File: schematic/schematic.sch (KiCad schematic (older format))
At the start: 22 parts, among them J1 Conn_01x04, J19 Conn_02x05_Odd_Even, J2 Conn_01x04, J20 Conn_02x05_Odd_Even, J21 Conn_02x05_Odd_Even, J3 Conn_01x04, J4 Conn_01x04, J5 Conn_01x04, SW1 SW_Push_Dual, U1 STM32F401VETx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

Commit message: Updated to kicad 5.0.0
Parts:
- C1, C2, C3, C4, C5: symbol C -> Device:C
- J1, J2, J3, J4, J5: symbol Conn_01x04 -> Connector_Generic:Conn_01x04
- J19, J20, J21: symbol Conn_02x05_Odd_Even -> Connector_Generic:Conn_02x05_Odd_Even
- MK1, MK2, MK3, MK4: symbol Mounting_Hole -> Mechanical:Mounting_Hole
- R1, R2: symbol R -> Device:R
- SW1: symbol SW_Push_Dual -> Switch:SW_Push_Dual
- U1: symbol STM32F401VETx -> MCU_ST_STM32:STM32F401VETx
- Y1: symbol Crystal_GND24 -> Device:Crystal_GND24
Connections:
- no-connect marks 4 -> 15

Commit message: Revert "Updated to kicad 5.0.0"
This reverts commit 6c14fa6c8e6361c9b9ee4065803a5a63755fc6a7.
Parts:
- C1, C2, C3, C4, C5: symbol Device:C -> C
- J1, J2, J3, J4, J5: symbol Connector_Generic:Conn_01x04 -> Conn_01x04
- J19, J20, J21: symbol Connector_Generic:Conn_02x05_Odd_Even -> Conn_02x05_Odd_Even
- MK1, MK2, MK3, MK4: symbol Mechanical:Mounting_Hole -> Mounting_Hole
- R1, R2: symbol Device:R -> R
- SW1: symbol Switch:SW_Push_Dual -> SW_Push_Dual
- U1: symbol MCU_ST_STM32:STM32F401VETx -> STM32F401VETx
- Y1: symbol Device:Crystal_GND24 -> Crystal_GND24
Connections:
- no-connect marks 15 -> 4

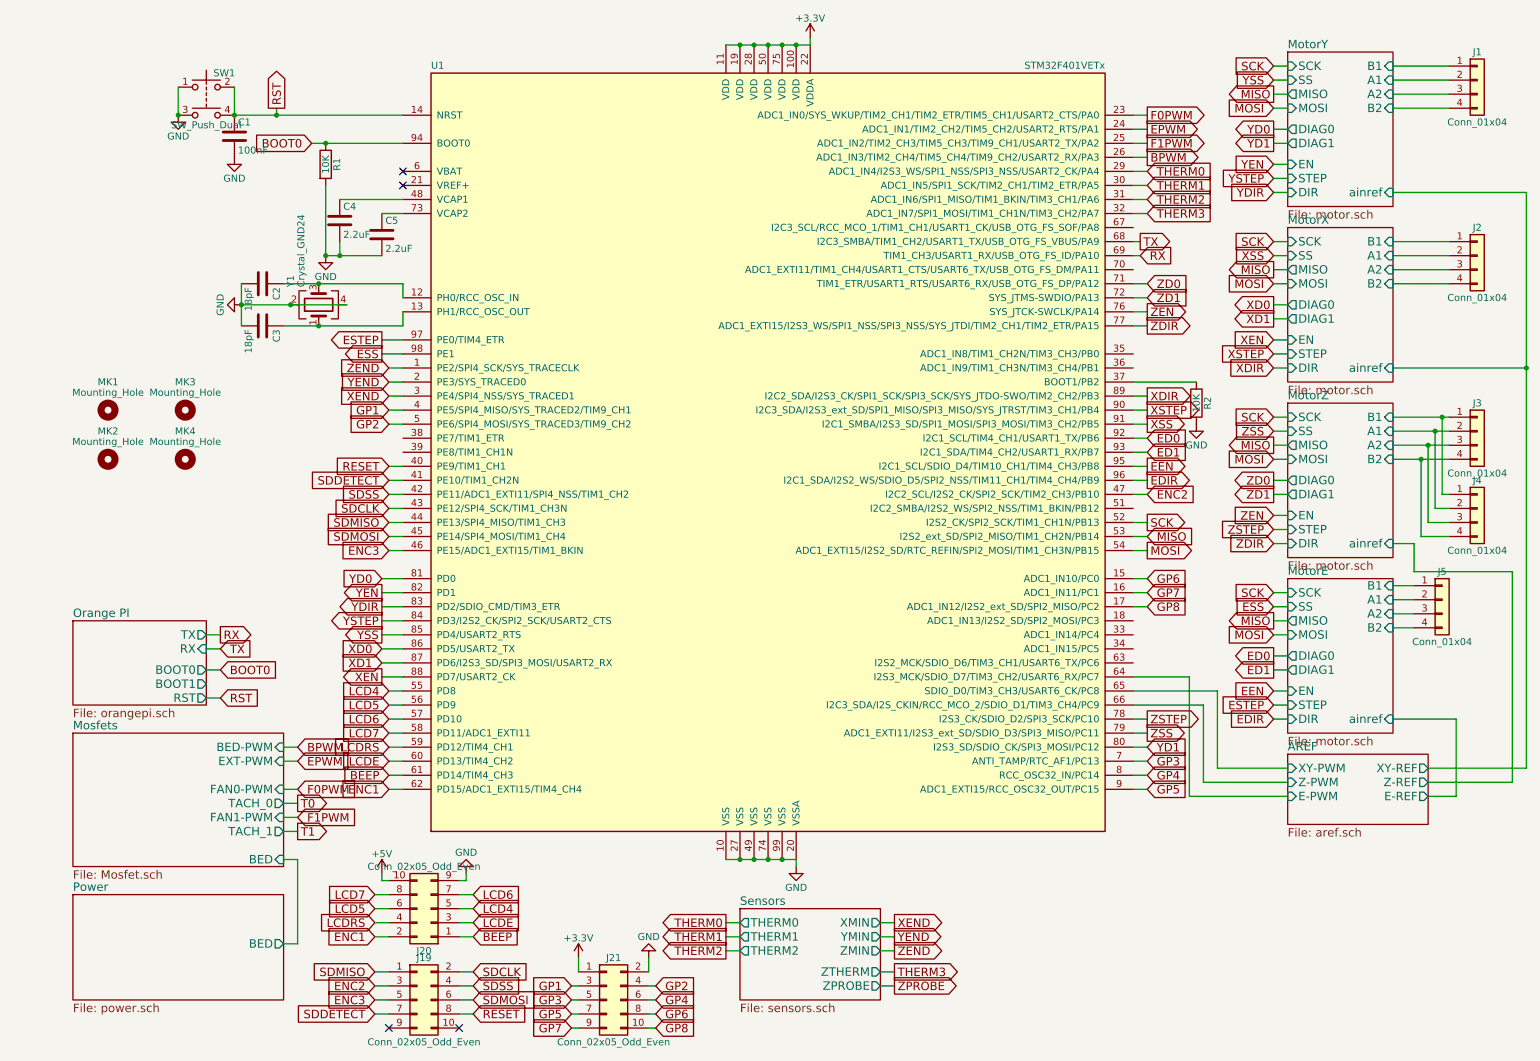
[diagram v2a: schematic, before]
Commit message: Removed some components
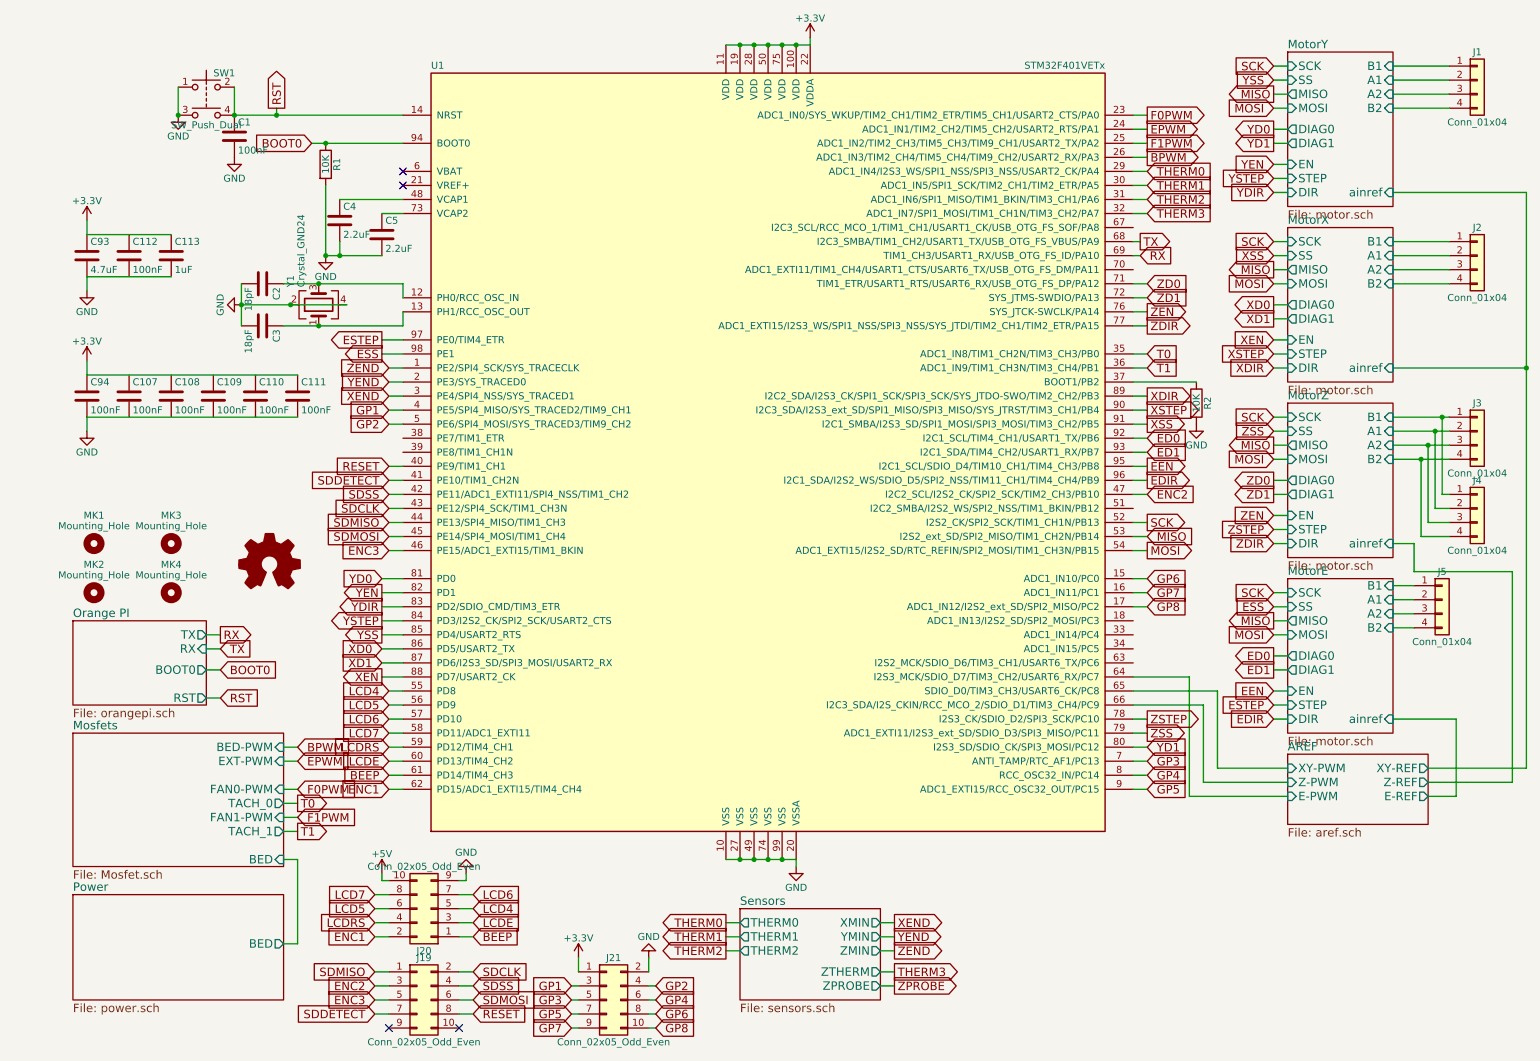
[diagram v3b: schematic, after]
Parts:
- added C107, C108, C109, C110, C111, C112: 100nF, Capacitors_SMD:C_0603, symbol C
- added C113: 1uF, Capacitors_SMD:C_0603, symbol C
- added C93: 4.7uF, Capacitors_SMD:C_0603, symbol C
- added C94: 100nF, Capacitor_SMD:C_0603_1608Metric, symbol C
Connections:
- net +3V3: now also C111.1, C113.1, C93.1, C94.1
- net GND: now also C111.2, C113.2, C93.2, C94.2
- net T0: now also U1.35 (ADC1_IN8/TIM1_CH2N/TIM3_CH3/PB0)
- net T1: now also U1.36 (ADC1_IN9/TIM1_CH3N/TIM3_CH4/PB1)
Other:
- moved on the sheet: MK1, MK2, MK3, MK4

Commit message: Added logo's and stm32 capacitors
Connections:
- net +3V3: now also C107.1, C108.1, C109.1, C110.1, C112.1, U1.21 (VREF+)
- net GND: now also C107.2, C108.2, C109.2, C110.2, C112.2
- no-connect marks 4 -> 3
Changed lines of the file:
@@
 EESchema Schematic File Version 2
+LIBS:bd9e302efj
+LIBS:psmn1
+LIBS:tmc2130
 LIBS:74xgxx
 LIBS:74xx
@@
 LIBS:zetex
 LIBS:Zilog
-LIBS:bd9e302efj
-LIBS:psmn1
-LIBS:tmc2130
 LIBS:schematic-cache
 EELAYER 25 0
@@
 $EndComp
 $Comp
-L GND #PWR11
+L GND #PWR01
 U 1 1 59F126EE
 P 5700 6500
-F 0 "#PWR11" H 5700 6250 50  0001 C CNN
+F 0 "#PWR01" H 5700 6250 50  0001 C CNN
 F 1 "GND" H 5700 6350 50  0000 C CNN
 F 2 "" H 5700 6500 50  0001 C CNN
@@
 $EndComp
 $Comp
-L +3.3V #PWR1
+L +3.3V #PWR02
 U 1 1 59F1505F
 P 5800 600
-F 0 "#PWR1" H 5800 450 50  0001 C CNN
+F 0 "#PWR02" H 5800 450 50  0001 C CNN
 F 1 "+3.3V" H 5800 740 50  0000 C CNN
 F 2 "" H 5800 600 50  0001 C CNN
@@
 $EndComp
 $Comp
-L GND #PWR7
+L GND #PWR03
 U 1 1 59EF5034
 P 1750 2500
-F 0 "#PWR7" H 1750 2250 50  0001 C CNN
+F 0 "#PWR03" H 1750 2250 50  0001 C CNN
 F 1 "GND" H 1750 2350 50  0000 C CNN
 F 2 "" H 1750 2500 50  0001 C CNN
@@
 $EndComp
 $Comp
-L GND #PWR5
+L GND #PWR04
 U 1 1 59F2A2E0
 P 2350 2150
-F 0 "#PWR5" H 2350 1900 50  0001 C CNN
+F 0 "#PWR04" H 2350 1900 50  0001 C CNN
 F 1 "GND" H 2350 2000 50  0000 C CNN
 F 2 "" H 2350 2150 50  0001 C CNN
@@
 $EndComp
 $Comp
-L GND #PWR9
+L GND #PWR05
 U 1 1 59F2ED55
 P 8550 3350
-F 0 "#PWR9" H 8550 3100 50  0001 C CNN
+F 0 "#PWR05" H 8550 3100 50  0001 C CNN
 F 1 "GND" H 8550 3200 50  0000 C CNN
 F 2 "" H 8550 3350 50  0001 C CNN
@@
 $EndComp
 $Comp
-L GND #PWR2
+L GND #PWR06
 U 1 1 59F30F85
 P 1300 1150
-F 0 "#PWR2" H 1300 900 50  0001 C CNN
+F 0 "#PWR06" H 1300 900 50  0001 C CNN
 F 1 "GND" H 1300 1000 50  0000 C CNN
 F 2 "" H 1300 1150 50  0001 C CNN
@@
 $EndComp
 $Comp
-L GND #PWR3
+L GND #PWR07
 U 1 1 59F319C0
 P 1700 1450
-F 0 "#PWR3" H 1700 1200 50  0001 C CNN
+F 0 "#PWR07" H 1700 1200 50  0001 C CNN
 F 1 "GND" H 1700 1300 50  0000 C CNN
 F 2 "" H 1700 1450 50  0001 C CNN
@@
 RST
 NoConn ~ 2900 1550
-NoConn ~ 2900 1650
 Text GLabel 8150 2050 2    60   Output ~ 0
 TX
@@
 $EndComp
 $Comp
-L +5V #PWR12
+L +5V #PWR08
 U 1 1 5A71CAE9
 P 2750 6550
-F 0 "#PWR12" H 2750 6400 50  0001 C CNN
+F 0 "#PWR08" H 2750 6400 50  0001 C CNN
 F 1 "+5V" H 2750 6690 50  0000 C CNN
 F 2 "" H 2750 6550 50  0001 C CNN
@@
 $EndComp
 $Comp
-L GND #PWR13
+L GND #PWR09
 U 1 1 5A71CE27
 P 3350 6550
-F 0 "#PWR13" H 3350 6300 50  0001 C CNN
+F 0 "#PWR09" H 3350 6300 50  0001 C CNN
 F 1 "GND" H 3350 6400 50  0000 C CNN
 F 2 "" H 3350 6550 50  0001 C CNN
@@
 $EndComp
 $Comp
-L +3.3V #PWR14
+L +3.3V #PWR010
 U 1 1 5A764DEA
 P 4150 7150
-F 0 "#PWR14" H 4150 7000 50  0001 C CNN
+F 0 "#PWR010" H 4150 7000 50  0001 C CNN
 F 1 "+3.3V" H 4150 7290 50  0000 C CNN
 F 2 "" H 4150 7150 50  0001 C CNN
@@
 $EndComp
 $Comp
-L GND #PWR15
+L GND #PWR011
 U 1 1 5A76523A
 P 4650 7150
-F 0 "#PWR15" H 4650 6900 50  0001 C CNN
+F 0 "#PWR011" H 4650 6900 50  0001 C CNN
 F 1 "GND" H 4650 7000 50  0000 C CNN
 F 2 "" H 4650 7150 50  0001 C CNN
@@
 	8100 2950 8200 2950
 $Comp
-L GND #PWR10
+L GND #PWR012
 U 1 1 5ADF511D
 P 650 3400
-F 0 "#PWR10" H 650 3150 50  0001 C CNN
+F 0 "#PWR012" H 650 3150 50  0001 C CNN
 F 1 "GND" H 650 3250 50  0000 C CNN
 F 2 "" H 650 3400 50  0001 C CNN
@@
 $EndComp
 $Comp
-L +3.3V #PWR8
+L +3.3V #PWR013
 U 1 1 5ADF71B2
 P 650 2900
-F 0 "#PWR8" H 650 2750 50  0001 C CNN
+F 0 "#PWR013" H 650 2750 50  0001 C CNN
 F 1 "+3.3V" H 650 3040 50  0000 C CNN
 F 2 "" H 650 2900 50  0001 C CNN
@@
 F 0 "#LOGO1" H 1950 4625 50  0001 C CNN
 F 1 "Logo_Open_Hardware_Small" H 1950 4125 50  0001 C CNN
-F 2 "" H 1950 4350 50  0001 C CNN
+F 2 "Symbols:OSHW-Logo_11.4x12mm_SilkScreen" H 1950 4350 50  0001 C CNN
 F 3 "" H 1950 4350 50  0001 C CNN
 	1    1950 4350
@@
 	650  3000 2150 3000
 $Comp
-L GND #PWR6
+L GND #PWR014
 U 1 1 5AE06323
 P 650 2400
-F 0 "#PWR6" H 650 2150 50  0001 C CNN
+F 0 "#PWR014" H 650 2150 50  0001 C CNN
 F 1 "GND" H 650 2250 50  0000 C CNN
 F 2 "" H 650 2400 50  0001 C CNN
@@
 $EndComp
 $Comp
-L +3.3V #PWR4
+L +3.3V #PWR015
 U 1 1 5AE06329
 P 650 1900
-F 0 "#PWR4" H 650 1750 50  0001 C CNN
+F 0 "#PWR015" H 650 1750 50  0001 C CNN
 F 1 "+3.3V" H 650 2040 50  0000 C CNN
 F 2 "" H 650 1900 50  0001 C CNN
@@
 Wire Wire Line
 	650  2300 1250 2300
+Connection ~ 650  3000
+Connection ~ 950  3000
+Connection ~ 1250 3000
+Connection ~ 1550 3000
+Connection ~ 1850 3000
+Connection ~ 950  3300
+Connection ~ 1250 3300
+Connection ~ 1550 3300
+Connection ~ 1850 3300
+Connection ~ 950  2000
+Connection ~ 950  2300
+Connection ~ 650  2000
+Connection ~ 650  2300
+Connection ~ 650  3300
+Wire Wire Line
+	2900 1650 2650 1650
+$Comp
+L +3.3V #PWR016
+U 1 1 5ADE5ADE
+P 2650 1650
+F 0 "#PWR016" H 2650 1500 50  0001 C CNN
+F 1 "+3.3V" H 2650 1790 50  0000 C CNN
+F 2 "" H 2650 1650 50  0001 C CNN
+F 3 "" H 2650 1650 50  0001 C CNN
+	1    2650 1650
+	1    0    0    -1
+$EndComp
 $EndSCHEMATC

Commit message: Saved schematic
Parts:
- C94: footprint Capacitor_SMD:C_0603_1608Metric -> Capacitors_SMD:C_0603
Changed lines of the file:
@@
 F 0 "C94" H 675 3250 50  0000 L CNN
 F 1 "100nF" H 675 3050 50  0000 L CNN
-F 2 "Capacitor_SMD:C_0603_1608Metric" H 688 3000 50  0001 C CNN
+F 2 "Capacitors_SMD:C_0603" H 688 3000 50  0001 C CNN
 F 3 "" H 650 3150 50  0001 C CNN
 	1    650  3150

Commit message: Updated to kicad v5
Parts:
- C1, C107, C108, C109, C110, C111, C112, C113, C2, C3, C4, C5, C93, C94: symbol C -> schematic-rescue:C
- J1, J2, J3, J4, J5: symbol Conn_01x04 -> schematic-rescue:Conn_01x04
- J19, J20, J21: symbol Conn_02x05_Odd_Even -> schematic-rescue:Conn_02x05_Odd_Even
- MK1, MK2, MK3, MK4: symbol Mounting_Hole -> schematic-rescue:Mounting_Hole
- R1, R2: symbol R -> schematic-rescue:R
- SW1: symbol SW_Push_Dual -> schematic-rescue:SW_Push_Dual
- U1: symbol STM32F401VETx -> schematic-rescue:STM32F401VETx
- Y1: symbol Crystal_GND24 -> schematic-rescue:Crystal_GND24

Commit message: Moved to L6470 driver
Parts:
- C1, C107, C108, C109, C110, C111, C112, C113, C2, C3, C93, C94: footprint Capacitors_SMD:C_0603 -> Capacitor_SMD:C_0603_1608Metric; symbol schematic-rescue:C -> Device:C
- C4, C5: footprint Capacitors_SMD:C_0805 -> Capacitor_SMD:C_0805_2012Metric; symbol schematic-rescue:C -> Device:C
- J1, J2, J3, J4, J5: footprint Socket_Strips:Socket_Strip_Straight_1x04_Pitch2.54mm -> Connector_PinHeader_2.54mm:PinHeader_1x04_P2.54mm_Vertical; symbol schematic-rescue:Conn_01x04 -> Connector_Generic:Conn_01x04
- J19, J20: footprint Connectors:IDC_Header_Straight_10pins -> Connector_IDC:IDC-Header_2x05_P2.54mm_Vertical; symbol schematic-rescue:Conn_02x05_Odd_Even -> Connector_Generic:Conn_02x05_Odd_Even
- J21: footprint Pin_Headers:Pin_Header_Straight_2x05_Pitch2.54mm -> Connector_IDC:IDC-Header_2x05_P2.54mm_Vertical; symbol schematic-rescue:Conn_02x05_Odd_Even -> Connector_Generic:Conn_02x05_Odd_Even
- MK1, MK2, MK3, MK4: footprint Mounting_Holes:MountingHole_3.2mm_M3 -> MountingHole:MountingHole_3.2mm_M3; symbol schematic-rescue:Mounting_Hole -> Mechanical:MountingHole
- R1, R2: footprint Resistors_SMD:R_0603 -> Resistor_SMD:R_0603_1608Metric; symbol schematic-rescue:R -> Device:R
- SW1: symbol schematic-rescue:SW_Push_Dual -> Switch:SW_Push_Dual
- U1: footprint Housings_QFP:TQFP-100_14x14mm_Pitch0.5mm -> Package_QFP:LQFP-100_14x14mm_P0.5mm
- Y1: footprint Crystals:Crystal_SMD_SeikoEpson_FA238-4pin_3.2x2.5mm_HandSoldering -> Crystal:Crystal_SMD_SeikoEpson_FA238-4Pin_3.2x2.5mm_HandSoldering; symbol schematic-rescue:Crystal_GND24 -> Device:Crystal_GND24
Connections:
- net labels removed: ED0, ED1, EDIR, EEN, ESTEP, XD0, XD1, XDIR, XEN, XSTEP, YD0, YD1, YDIR, YEN, YSTEP, ZD0, ZD1, ZDIR, ZEN, ZSTEP
- wire segments 259 -> 216
